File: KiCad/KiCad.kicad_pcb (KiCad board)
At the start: 2 copper layers, 1 part, among them U1 ESP32-WROOM-32E

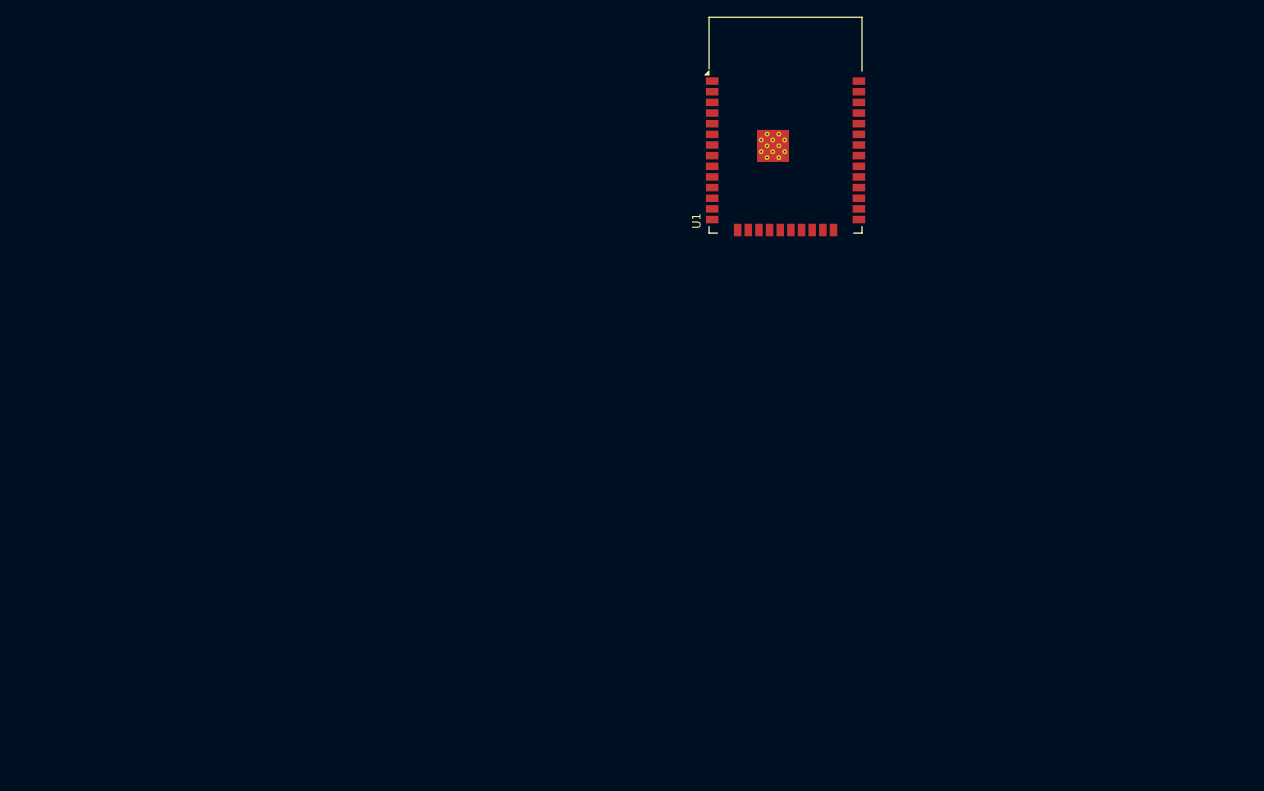
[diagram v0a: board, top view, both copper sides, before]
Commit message: 完成主電源輸入轉到數位系統主電源軌電壓(12~24v to 5v)之原理圖，包含外部DC供電接口
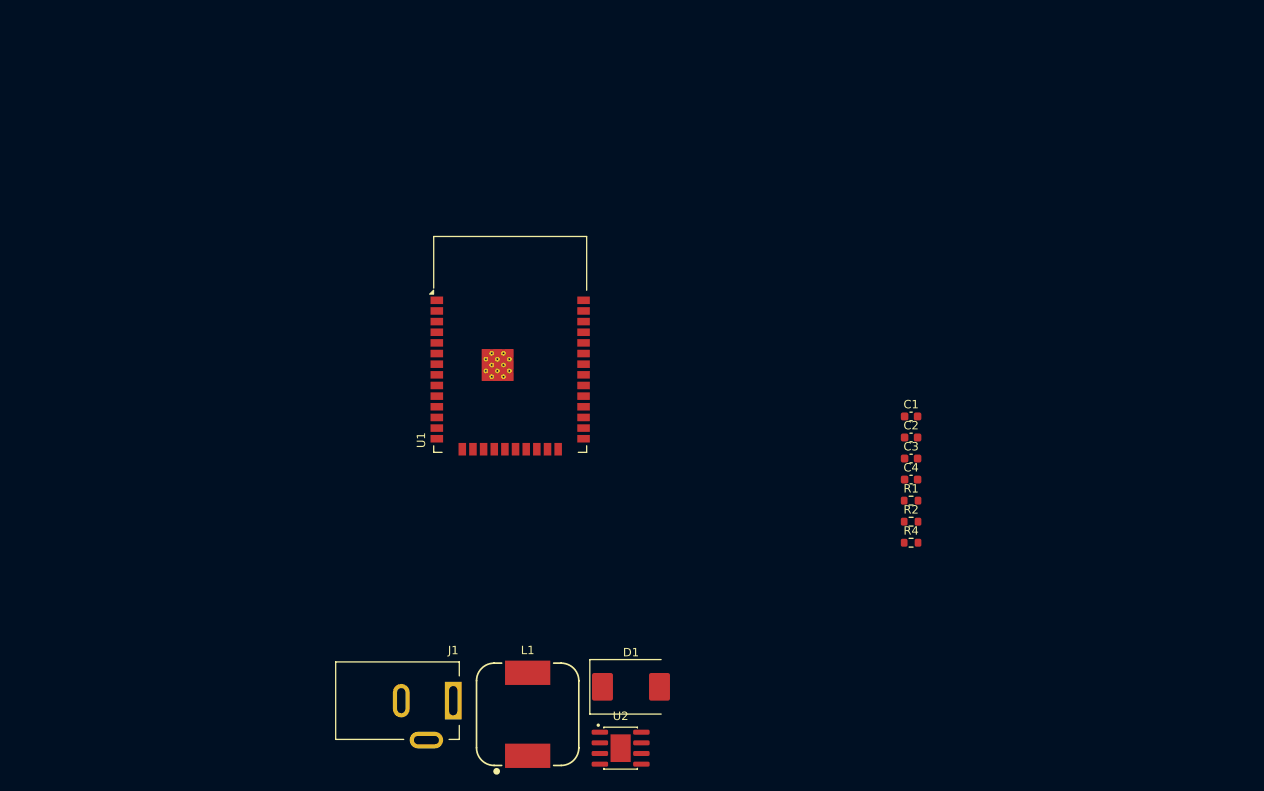
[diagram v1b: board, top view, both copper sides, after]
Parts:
- added C1: C, Capacitor_SMD:C_0603_1608Metric, F.Cu at (227.2, 100.0)
- added C2: C, Capacitor_SMD:C_0603_1608Metric, F.Cu at (227.2, 102.5)
- added C3: C, Capacitor_SMD:C_0603_1608Metric, F.Cu at (227.2, 105.0)
- added C4: C, Capacitor_SMD:C_0603_1608Metric, F.Cu at (227.2, 107.5)
- added D1: B340, Diode_SMD:D_SMC, F.Cu at (193.8, 132.2)
- added J1: Barrel_Jack_MountingPin, Connector_BarrelJack:BarrelJack_Kycon_KLDX-0202-xC_Horizontal, F.Cu at (172.6, 133.9)
- added L1: WE-PD_1260, DC-DC POWER L1:WE-PD_1260, F.Cu at (181.5, 135.5)
- added R1: R, Resistor_SMD:R_0603_1608Metric, F.Cu at (227.2, 110.0)
- added R2: R, Resistor_SMD:R_0603_1608Metric, F.Cu at (227.2, 112.5)
- added R4: R, Resistor_SMD:R_0603_1608Metric, F.Cu at (227.2, 115.0)
- added U2: MP1584EN, MP1584:SOIC127P600X170-9N, F.Cu at (192.6, 139.5)
- moved U1 42.0 mm to (179.4, 94.4)

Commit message: 完成主電源輸入轉到數位系統主電源軌電壓模塊(12~24v to 5v)之PCB
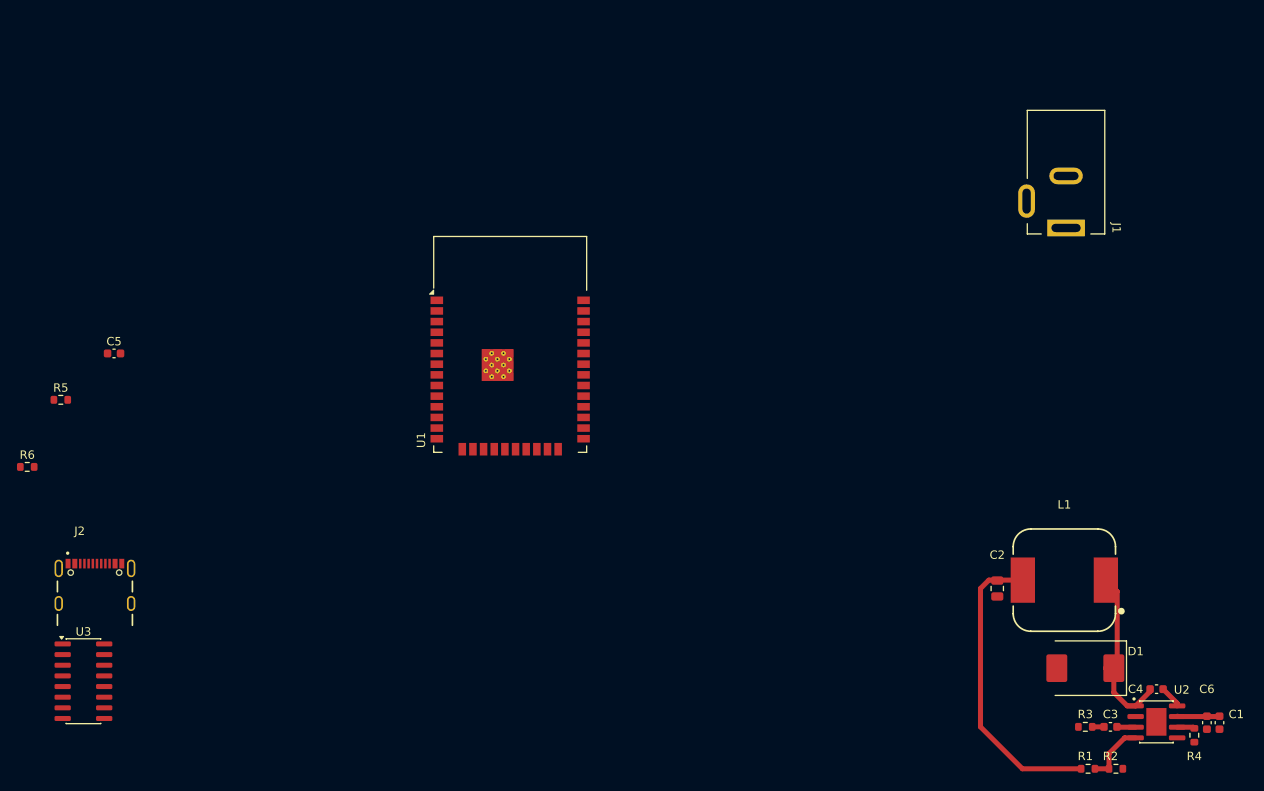
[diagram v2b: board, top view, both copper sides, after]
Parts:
- added C5: 0.1uF, Capacitor_SMD:C_0603_1608Metric, F.Cu at (132.2, 92.5)
- added C6: 0.1uF, Capacitor_SMD:C_0603_1608Metric, F.Cu at (262.5, 136.5)
- added J2: USB4105-GF-A, USB4105-GF-A:GCT_USB4105-GF-A, F.Cu at (129.9, 122.3)
- added R3: 100K, Resistor_SMD:R_0603_1608Metric, F.Cu at (248.0, 137.0)
- added R5: 5.1K, Resistor_SMD:R_0603_1608Metric, F.Cu at (125.8, 98.0)
- added R6: 5.1K, Resistor_SMD:R_0603_1608Metric, F.Cu at (121.8, 106.0)
- added U3: CH340C, Package_SO:SOIC-16_3.9x9.9mm_P1.27mm, F.Cu at (128.5, 131.6)
- C1: value C -> 10uF
- C2: value C -> 22uF; footprint Capacitor_SMD:C_0603_1608Metric -> Capacitor_SMD:C_0805_2012Metric
- C3: value C -> 150pF
- C4: value C -> 0.1uF
- L1: value WE-PD_1260 -> 22uH
- R1: value R -> 210K
- R2: value R -> 40.2K
- R4: value R -> 200K
- moved J1 92.3 mm to (245.7, 77.5), turned to -90 degrees
- moved L1 66.0 mm to (245.5, 119.5), turned to 90 degrees
- moved U2 64.0 mm to (256.5, 136.4)
- moved D1 54.2 mm to (248.0, 130.0), turned to 180 degrees
- moved C1 51.8 mm to (264.0, 136.5), turned to -90 degrees
- moved R4 40.8 mm to (261.0, 138.0), turned to -90 degrees
- moved C3 39.9 mm to (251.0, 137.0), turned to 180 degrees
- moved C4 38.5 mm to (256.5, 132.5), turned to 180 degrees
- moved R1 38.3 mm to (248.3, 142.0)
- moved R2 38.3 mm to (251.7, 142.0)
- moved C2 20.7 mm to (237.5, 120.5), turned to -90 degrees
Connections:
- U1 pad 34: unconnected-(U1-RXD0/IO3-Pad34) -> /ESP32_RX
- U1 pad 35: unconnected-(U1-TXD0/IO1-Pad35) -> /ESP32_TX
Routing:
- net +5V: track 0.00 -> 36.0 mm
- net Net-(D1-K): track 0.00 -> 21.4 mm
- net Net-(U2-FB): track 0.00 -> 7.45 mm
- net VCC: track 0.00 -> 5.13 mm
- net Net-(U2-BST): track 0.00 -> 2.69 mm
- net Net-(U2-COMP): track 0.00 -> 2.24 mm
- net Net-(U2-FREQ): track 0.00 -> 2.11 mm
- net Net-(C3-Pad2): track 0.00 -> 1.40 mm

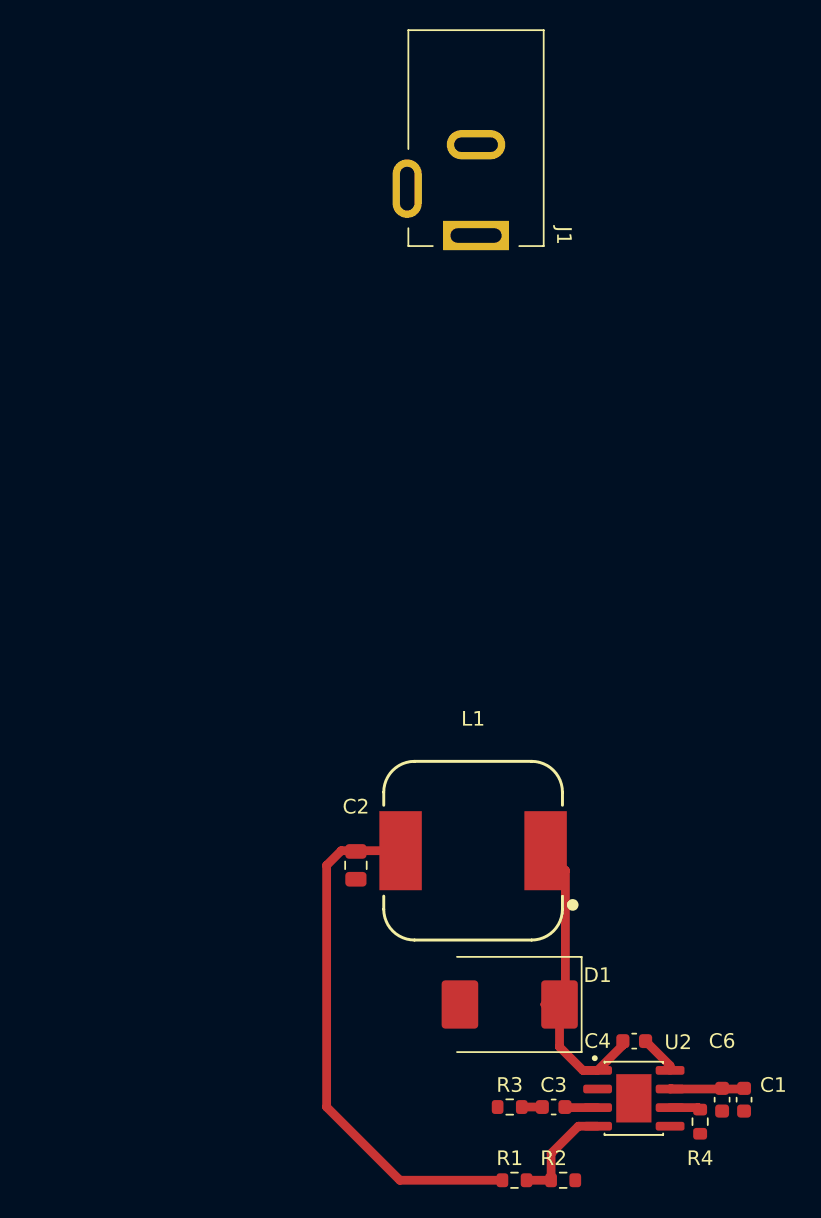
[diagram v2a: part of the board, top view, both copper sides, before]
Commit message: 完成5v電源軌的所有電路
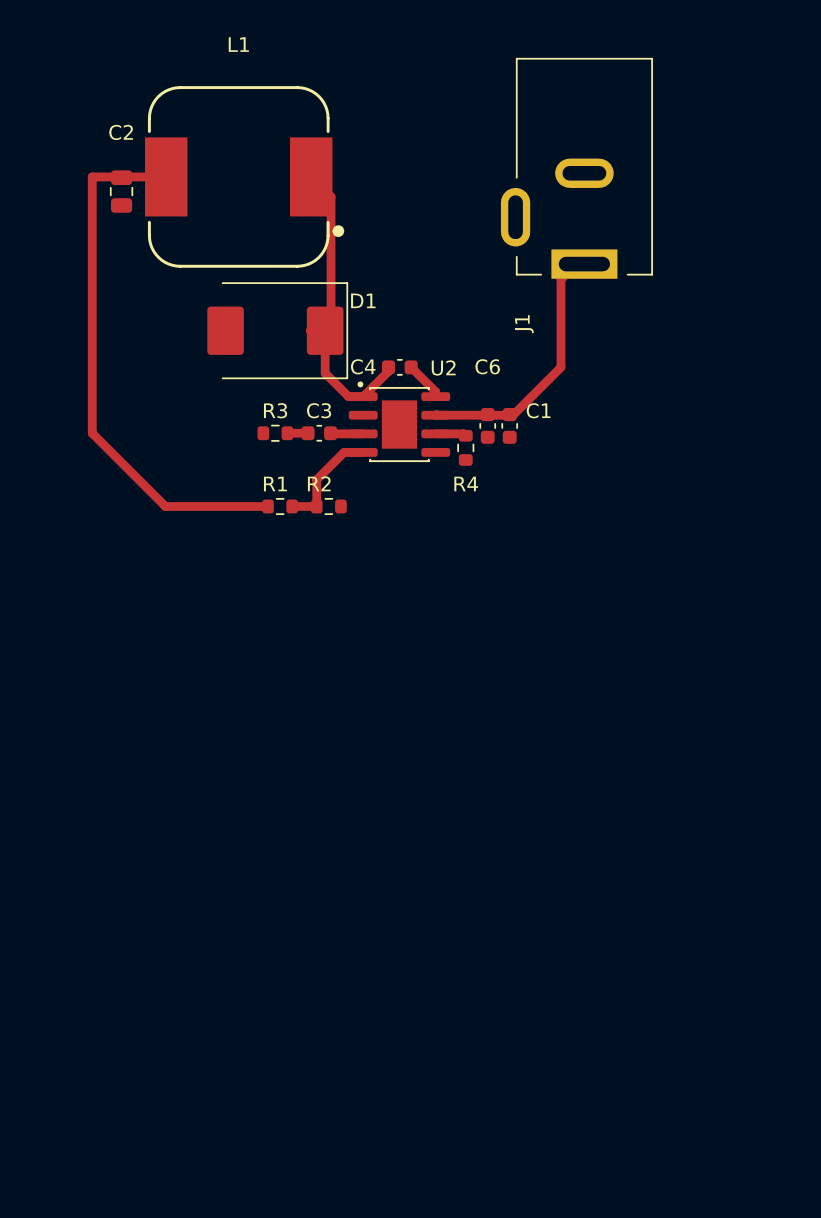
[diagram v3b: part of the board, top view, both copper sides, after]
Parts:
- J1: value Barrel_Jack_MountingPin -> DC-IN
- moved U2 48.7 mm to (240.5, 90.4)
- moved C1 48.7 mm to (248.0, 90.5)
- moved C2 48.7 mm to (221.5, 74.5)
- moved C3 48.7 mm to (235.0, 91.0)
- moved C4 48.7 mm to (240.5, 86.5)
- moved C6 48.7 mm to (246.5, 90.5)
- moved D1 48.7 mm to (232.0, 84.0)
- moved L1 48.7 mm to (229.5, 73.5)
- moved R1 48.7 mm to (232.3, 96.0)
- moved R2 48.7 mm to (235.7, 96.0)
- moved R3 48.7 mm to (232.0, 91.0)
- moved R4 48.7 mm to (245.0, 92.0)
- moved J1 7.65 mm to (253.1, 79.5)
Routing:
- net VCC: track 5.13 -> 18.8 mm
- net +5V: track 36.0 -> 36.6 mm

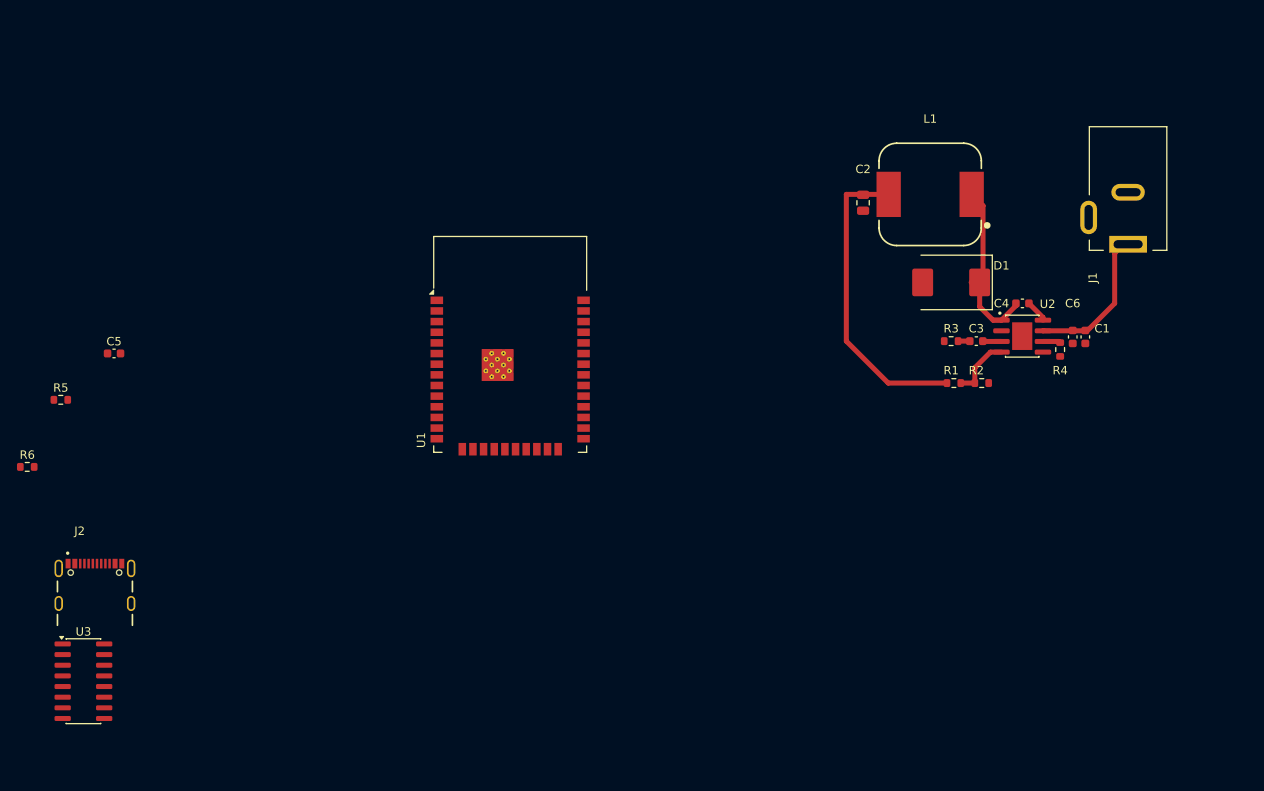
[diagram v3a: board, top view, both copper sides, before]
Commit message: 完成5V轉3.3V電源軌元件及防反接電路、ESP32復位電路、優化主電源輸入轉5V的電路、USB轉TTL完整迴路之原理突及PCB
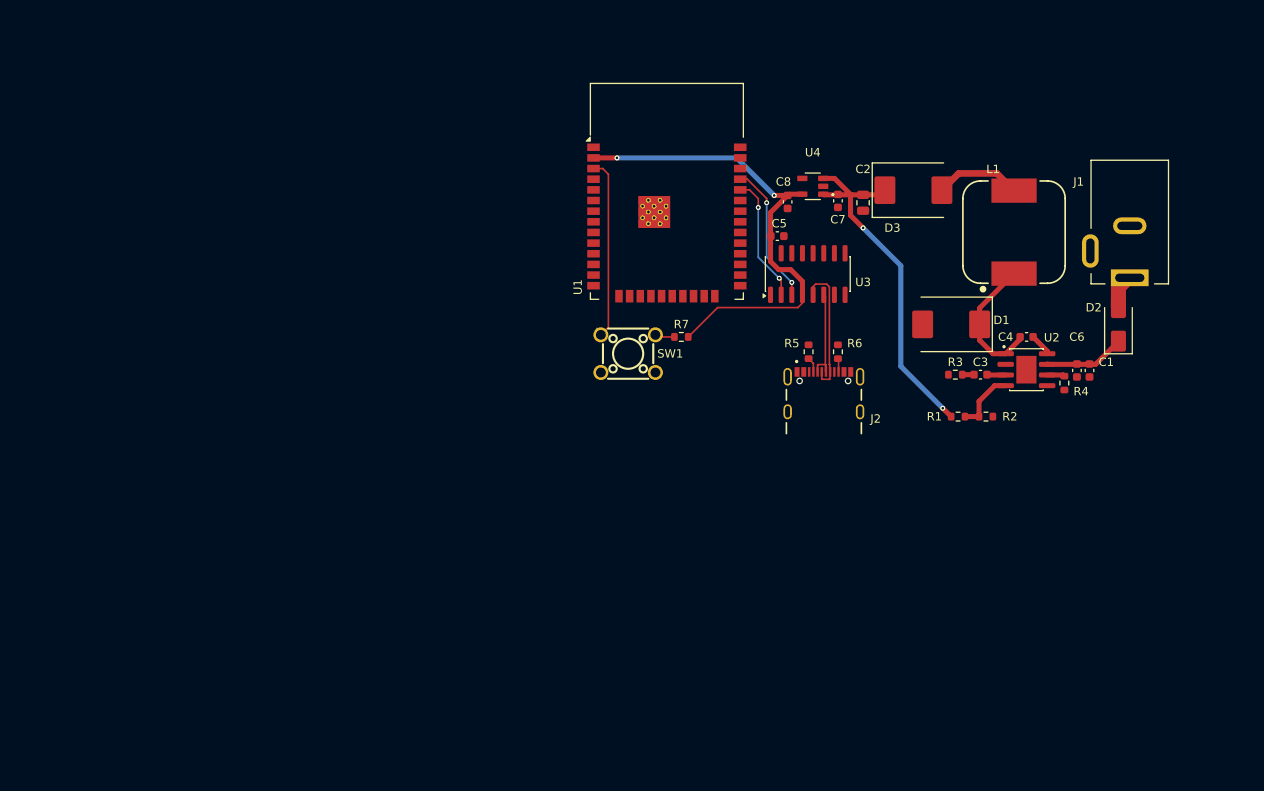
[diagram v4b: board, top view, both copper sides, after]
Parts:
- added C7: 1uF, Capacitor_SMD:C_0603_1608Metric, F.Cu at (218.5, 74.3)
- added C8: 1uF, Capacitor_SMD:C_0603_1608Metric, F.Cu at (212.5, 74.4)
- added D2: SS14, Diode_SMD:D_SMA, F.Cu at (251.9, 89.0)
- added D3: B340, Diode_SMD:D_SMC, F.Cu at (227.5, 73.0)
- added R7: 5.1K, Resistor_SMD:R_0603_1608Metric, F.Cu at (199.8, 90.5)
- added SW1: TS665CJ, button:SW-TH_4P-L6.0-W6.0-P4.50-LS6.5, F.Cu at (193.5, 92.5)
- added U4: RT9013-33GB, RT9013-33GB:SOT94P279X129-5N, F.Cu at (215.5, 72.5)
- J2: value USB4105-GF-A -> TYPE-C
- L1: value 22uH -> 15uH
- moved U3 99.1 mm to (214.9, 83.0), turned to 90 degrees
- moved R6 97.6 mm to (218.5, 92.3), turned to 90 degrees
- moved J2 89.9 mm to (216.8, 99.4)
- moved R5 89.4 mm to (215.0, 92.3), turned to 90 degrees
- moved C5 80.3 mm to (211.3, 78.5)
- moved U1 26.1 mm to (198.1, 76.1)
- moved L1 11.0 mm to (239.5, 78.0), turned to 0 degrees
- moved D1 5.00 mm to (232.0, 89.0)
- moved C1 4.03 mm to (248.5, 94.5)
- moved C3 4.03 mm to (235.5, 95.0)
- moved C4 4.03 mm to (241.0, 90.5)
- moved C6 4.03 mm to (247.0, 94.5)
- moved R1 4.03 mm to (232.8, 100.0)
- moved R2 4.03 mm to (236.2, 100.0)
- moved R3 4.03 mm to (232.5, 95.0)
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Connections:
- C1 pad 1: VCC -> Net-(D2-K)
- C6 pad 1: VCC -> Net-(D2-K)
- L1 pad 2: +5V -> Net-(D3-A)
- U1 pad 3: unconnected-(U1-EN-Pad3) -> Net-(SW1-A)
- U2 pad 7: VCC -> Net-(D2-K)
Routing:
- net +3V3: track 0.00 -> 57.9 mm, vias 0 -> 2
- net Net-(SW1-A): track 0.00 -> 23.8 mm
- net /ESP32_TX: track 0.00 -> 16.8 mm, vias 0 -> 2
- net /D+: track 0.00 -> 16.0 mm
- net /ESP32_RX: track 0.00 -> 15.2 mm, vias 0 -> 2
- net VCC: track 18.8 -> 4.56 mm
- net /D-: track 0.00 -> 12.0 mm
- net Net-(D3-A): track 0.00 -> 10.3 mm
- net Net-(D2-K): track 0.00 -> 9.71 mm
- net +5V: track 36.6 -> 43.2 mm, vias 0 -> 2
- net Net-(D1-K): track 21.4 -> 17.0 mm
- net Net-(J2-CC1): track 0.00 -> 1.82 mm
- net Net-(J2-CC2): track 0.00 -> 1.61 mm
